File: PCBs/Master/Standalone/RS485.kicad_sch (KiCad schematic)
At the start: 16 parts, among them U4 TBU-CA065-200-WH, U5 TBU-CA065-200-WH, U6 TISP4240M3BJR-S, U7 MAX487ESA+T, U8 MAX487ESA+T, U9 TISP4240M3BJR-S

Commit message: Master WIP
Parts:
- R10: footprint Resistor_SMD:R_0805_2012Metric -> Resistor_SMD:R_0402_1005Metric; LCSC C22978 -> C25890
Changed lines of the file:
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@@
     (property "Reference" "R10" (id 0) (at 173.99 128.27 90))
     (property "Value" "3.3K" (id 1) (at 173.99 130.81 90))
-    (property "Footprint" "Resistor_SMD:R_0805_2012Metric" (id 2) (at 173.99 132.842 90)
+    (property "Footprint" "Resistor_SMD:R_0402_1005Metric" (id 2) (at 173.99 132.842 90)
       (effects (font (size 1.27 1.27)) hide)
     )
@@
       (effects (font (size 1.27 1.27)) hide)
     )
-    (property "LCSC" "C22978" (id 4) (at 173.99 134.62 0)
+    (property "LCSC" "C25890" (id 4) (at 173.99 134.62 0)
       (effects (font (size 1.27 1.27)) hide)
     )

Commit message: Master Rev. 1
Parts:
- removed U6, U9: TISP4240M3BJR-S, A10 KiCad Libraries:DO-214AA_L4.4-W3.6-LS5.3-BI, symbol A10:TISP4240M3BJR-S
- F4: footprint A10 KiCad Libraries:FUSE_BK-6013 -> A10 KiCad Libraries:FUSE-TH_XF-506P
- U4, U5: now left out of the parts list
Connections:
- net RS485+: now also D6.1 (A1), F3.1
- net RS485-: now also D6.2 (A2), F2.2
- now unconnected: U4.1 (IN/OUT), U5.3 (OUT/IN)
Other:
- moved on the sheet: U4, U5
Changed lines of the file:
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@@
   (junction (at 97.79 106.68) (diameter 0) (color 0 0 0 0)
   )
-  (no_connect (at 154.94 97.79))
-  (no_connect (at 154.94 113.03))
+  (no_connect (at 157.48 97.79))
+  (no_connect (at 157.48 113.03))
   (wire (pts (xy 143.51 96.52) (xy 154.94 95.25))
     (stroke (width 0) (type default) (color 0 0 0 0))
@@
     (stroke (width 0) (type default) (color 0 0 0 0))
   )
-  (wire (pts (xy 185.42 106.68) (xy 154.94 106.68))
-    (stroke (width 0) (type default) (color 0 0 0 0))
-  )
   (wire (pts (xy 116.84 128.27) (xy 116.84 130.81))
     (stroke (width 0) (type default) (color 0 0 0 0))
   )
-  (wire (pts (xy 154.94 106.68) (xy 154.94 110.49))
-    (stroke (width 0) (type default) (color 0 0 0 0))
-  )
   (wire (pts (xy 166.37 134.62) (xy 170.18 134.62))
     (stroke (width 0) (type default) (color 0 0 0 0))
@@
     (stroke (width 0) (type default) (color 0 0 0 0))
   )
-  (wire (pts (xy 185.42 104.14) (xy 207.01 104.14))
+  (wire (pts (xy 154.94 104.14) (xy 185.42 104.14))
     (stroke (width 0) (type default) (color 0 0 0 0))
   )
@@
     (stroke (width 0) (type default) (color 0 0 0 0))
   )
-  (wire (pts (xy 195.58 106.68) (xy 207.01 106.68))
-    (stroke (width 0) (type default) (color 0 0 0 0))
-  )
-  (wire (pts (xy 154.94 100.33) (xy 154.94 104.14))
+  (wire (pts (xy 154.94 106.68) (xy 185.42 106.68))
+    (stroke (width 0) (type default) (color 0 0 0 0))
+  )
+  (wire (pts (xy 154.94 95.25) (xy 154.94 104.14))
     (stroke (width 0) (type default) (color 0 0 0 0))
   )
@@
     (stroke (width 0) (type default) (color 0 0 0 0))
   )
+  (wire (pts (xy 154.94 106.68) (xy 154.94 115.57))
+    (stroke (width 0) (type default) (color 0 0 0 0))
+  )
   (wire (pts (xy 107.95 83.82) (xy 107.95 87.63))
     (stroke (width 0) (type default) (color 0 0 0 0))
@@
   )
   (wire (pts (xy 168.91 139.7) (xy 166.37 139.7))
-    (stroke (width 0) (type default) (color 0 0 0 0))
-  )
-  (wire (pts (xy 154.94 104.14) (xy 175.26 104.14))
     (stroke (width 0) (type default) (color 0 0 0 0))
   )
@@
     )
   )
-  (global_label "RS485+" (shape bidirectional) (at 207.01 106.68 0) (fields_autoplaced)
+  (global_label "RS485+" (shape bidirectional) (at 185.42 106.68 0) (fields_autoplaced)
     (effects (font (size 1.27 1.27)) (justify left))
-    (property "Intersheet References" "${INTERSHEET_REFS}" (id 0) (at 217.1036 106.7594 0)
+    (property "Intersheet References" "${INTERSHEET_REFS}" (id 0) (at 195.5136 106.7594 0)
       (effects (font (size 1.27 1.27)) (justify left) hide)
     )
@@
     )
   )
-  (global_label "RS485-" (shape bidirectional) (at 207.01 104.14 0) (fields_autoplaced)
+  (global_label "RS485-" (shape bidirectional) (at 185.42 104.14 0) (fields_autoplaced)
     (effects (font (size 1.27 1.27)) (justify left))
-    (property "Intersheet References" "${INTERSHEET_REFS}" (id 0) (at 217.1036 104.2194 0)
+    (property "Intersheet References" "${INTERSHEET_REFS}" (id 0) (at 195.5136 104.2194 0)
       (effects (font (size 1.27 1.27)) (justify left) hide)
     )
@@
     (effects (font (size 1.27 1.27)) (justify right))
   )
-  (hierarchical_label "RS485-" (shape output) (at 204.47 104.14 90)
+  (hierarchical_label "RS485-" (shape output) (at 182.88 104.14 90)
     (effects (font (size 1.27 1.27)) (justify left))
   )
-  (hierarchical_label "RS485+" (shape output) (at 204.47 106.68 270)
+  (hierarchical_label "RS485+" (shape output) (at 182.88 106.68 270)
     (effects (font (size 1.27 1.27)) (justify right))
   )
@@
     (pin "2")
     (pin "3")
-  )
-  (symbol (lib_id "A10:TISP4240M3BJR-S") (at 187.96 99.06 0) (unit 1)
-    (in_bom yes) (on_board yes)
-    (property "Reference" "U6" (id 0) (at 190.5 110.49 0))
-    (property "Value" "TISP4240M3BJR-S" (id 1) (at 190.5 113.03 0))
-    (property "Footprint" "A10 KiCad Libraries:DO-214AA_L4.4-W3.6-LS5.3-BI" (id 2) (at 187.96 109.22 0)
-      (effects (font (size 1.27 1.27) italic) hide)
-    )
-    (property "Datasheet" "https://atta.szlcsc.com/upload/public/pdf/source/20210316/C2760879_B8B4F1F8D05F3CAAD32384151EC07A7F.pdf" (id 3) (at 185.674 98.933 0)
-      (effects (font (size 1.27 1.27)) (justify left) hide)
-    )
-    (property "LCSC" "C840526" (id 4) (at 187.96 99.06 0)
-      (effects (font (size 1.27 1.27)) hide)
-    )
-    (pin "1")
-    (pin "2")
   )
   (symbol (lib_id "Connector_Generic:Conn_02x02_Odd_Even") (at 121.92 128.27 0) (unit 1)
@@
     (pin "4")
   )
-  (symbol (lib_name "TBU-CA065-200-WH_1") (lib_id "A10:TBU-CA065-200-WH") (at 154.94 74.93 0) (unit 1)
-    (in_bom yes) (on_board yes)
-    (property "Reference" "U4" (id 0) (at 157.48 87.63 0)
-      (effects (font (size 1.27 1.27)) (justify left))
-    )
-    (property "Value" "TBU-CA065-200-WH" (id 1) (at 157.48 90.17 0)
-      (effects (font (size 1.27 1.27)) (justify left))
-    )
-    (property "Footprint" "A10 KiCad Libraries:DIO-SMD_3P-L6.5-W4.0-BI" (id 2) (at 154.94 85.09 0)
+  (symbol (lib_name "TBU-CA065-200-WH_1") (lib_id "A10:TBU-CA065-200-WH") (at 157.48 74.93 0) (unit 1)
+    (in_bom no) (on_board no)
+    (property "Reference" "U4" (id 0) (at 160.02 87.63 0)
+      (effects (font (size 1.27 1.27)) (justify left))
+    )
+    (property "Value" "TBU-CA065-200-WH" (id 1) (at 160.02 90.17 0)
+      (effects (font (size 1.27 1.27)) (justify left))
+    )
+    (property "Footprint" "A10 KiCad Libraries:DIO-SMD_3P-L6.5-W4.0-BI" (id 2) (at 157.48 85.09 0)
       (effects (font (size 1.27 1.27) italic) hide)
     )
-    (property "Datasheet" "https://atta.szlcsc.com/upload/public/pdf/source/20200810/C720638_9C2F93931169B2F615A5326102BC91F1.pdf" (id 3) (at 152.654 74.803 0)
-      (effects (font (size 1.27 1.27)) (justify left) hide)
-    )
-    (property "LCSC" "C913221" (id 4) (at 154.94 74.93 0)
+    (property "Datasheet" "https://atta.szlcsc.com/upload/public/pdf/source/20200810/C720638_9C2F93931169B2F615A5326102BC91F1.pdf" (id 3) (at 155.194 74.803 0)
+      (effects (font (size 1.27 1.27)) (justify left) hide)
+    )
+    (property "LCSC" "C913221" (id 4) (at 157.48 74.93 0)
       (effects (font (size 1.27 1.27)) hide)
     )
@@
     (pin "8")
   )
-  (symbol (lib_id "A10:TISP4240M3BJR-S") (at 182.88 111.76 180) (unit 1)
-    (in_bom yes) (on_board yes) (fields_autoplaced)
-    (property "Reference" "U9" (id 0) (at 180.34 99.06 0))
-    (property "Value" "TISP4240M3BJR-S" (id 1) (at 180.34 101.6 0))
-    (property "Footprint" "A10 KiCad Libraries:DO-214AA_L4.4-W3.6-LS5.3-BI" (id 2) (at 182.88 101.6 0)
-      (effects (font (size 1.27 1.27) italic) hide)
-    )
-    (property "Datasheet" "https://atta.szlcsc.com/upload/public/pdf/source/20210316/C2760879_B8B4F1F8D05F3CAAD32384151EC07A7F.pdf" (id 3) (at 185.166 111.887 0)
-      (effects (font (size 1.27 1.27)) (justify left) hide)
-    )
-    (property "LCSC" "C840526" (id 4) (at 182.88 111.76 0)
-      (effects (font (size 1.27 1.27)) hide)
-    )
-    (pin "1")
-    (pin "2")
-  )
   (symbol (lib_id "power:GND") (at 124.46 87.63 90) (unit 1)
     (in_bom yes) (on_board yes) (fields_autoplaced)
@@
       (effects (font (size 1.27 1.27)) (justify left))
     )
-    (property "Footprint" "A10 KiCad Libraries:FUSE_BK-6013" (id 2) (at 140.97 136.398 90)
+    (property "Footprint" "A10 KiCad Libraries:FUSE-TH_XF-506P" (id 2) (at 140.97 136.398 90)
       (effects (font (size 1.27 1.27)) hide)
     )
@@
     (pin "8")
   )
-  (symbol (lib_name "TBU-CA065-200-WH_1") (lib_id "A10:TBU-CA065-200-WH") (at 154.94 90.17 0) (unit 1)
-    (in_bom yes) (on_board yes)
-    (property "Reference" "U5" (id 0) (at 157.48 120.65 0)
-      (effects (font (size 1.27 1.27)) (justify left))
-    )
-    (property "Value" "TBU-CA065-200-WH" (id 1) (at 157.48 123.19 0)
-      (effects (font (size 1.27 1.27)) (justify left))
-    )
-    (property "Footprint" "A10 KiCad Libraries:DIO-SMD_3P-L6.5-W4.0-BI" (id 2) (at 154.94 100.33 0)
+  (symbol (lib_name "TBU-CA065-200-WH_1") (lib_id "A10:TBU-CA065-200-WH") (at 157.48 90.17 0) (unit 1)
+    (in_bom no) (on_board no)
+    (property "Reference" "U5" (id 0) (at 160.02 120.65 0)
+      (effects (font (size 1.27 1.27)) (justify left))
+    )
+    (property "Value" "TBU-CA065-200-WH" (id 1) (at 160.02 123.19 0)
+      (effects (font (size 1.27 1.27)) (justify left))
+    )
+    (property "Footprint" "A10 KiCad Libraries:DIO-SMD_3P-L6.5-W4.0-BI" (id 2) (at 157.48 100.33 0)
       (effects (font (size 1.27 1.27) italic) hide)
     )
-    (property "Datasheet" "https://atta.szlcsc.com/upload/public/pdf/source/20200810/C720638_9C2F93931169B2F615A5326102BC91F1.pdf" (id 3) (at 152.654 90.043 0)
-      (effects (font (size 1.27 1.27)) (justify left) hide)
-    )
-    (property "LCSC" "C913221" (id 4) (at 154.94 90.17 0)
-      (effects (font (size 1.27 1.27)) hide)
-    )
+    (property "Datasheet" "https://atta.szlcsc.com/upload/public/pdf/source/20200810/C720638_9C2F93931169B2F615A5326102BC91F1.pdf" (id 3) (at 155.194 90.043 0)
+      (effects (font (size 1.27 1.27)) (justify left) hide)
+    )
+    (property "LCSC" "C913221" (id 4) (at 157.48 90.17 0)
+      (effects (font (size 1.27 1.27)) hide)
+    )

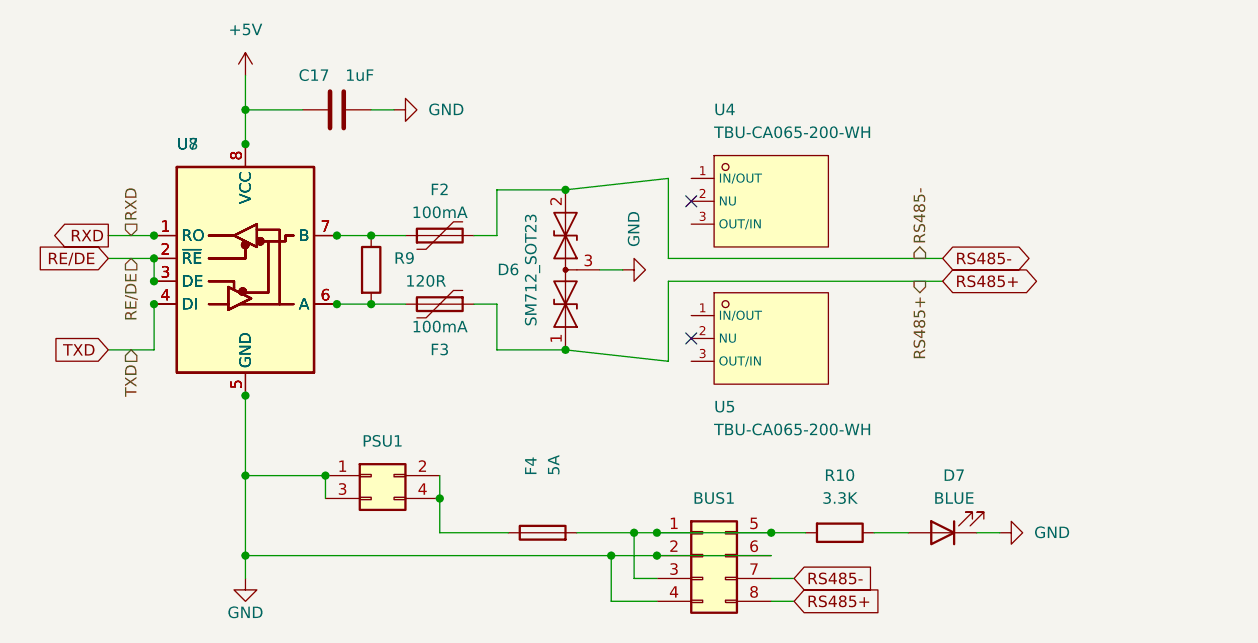
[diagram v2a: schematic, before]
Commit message: Updated Master to use PCIe Power Directly
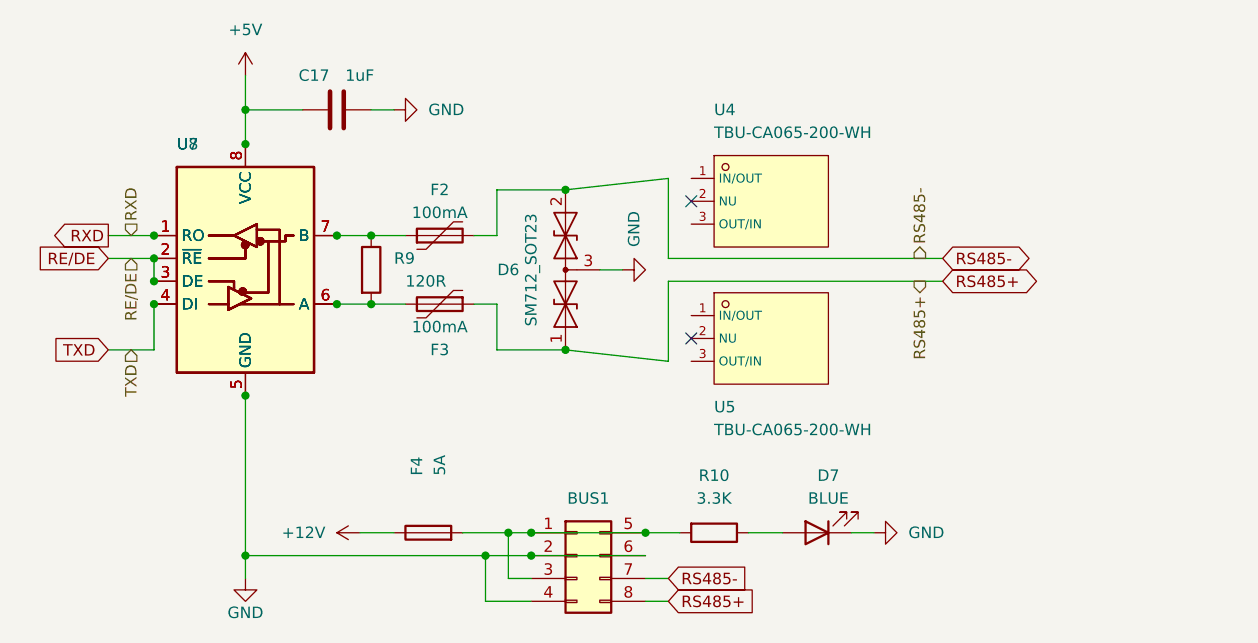
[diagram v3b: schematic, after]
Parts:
- removed PSU1: Conn_02x02_Top_Bottom, A10 KiCad Libraries:Molex Micro-Fit 3.0 43045-0400, symbol Connector_Generic:Conn_02x02_Odd_Even
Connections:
- net +12V: now reaches F4.1
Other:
- moved on the sheet: BUS1, D7, F4, R10

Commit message: Updated HUB
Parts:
- F4: now in the parts list
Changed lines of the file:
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@@
   )
   (symbol (lib_id "Device:Fuse") (at 128.27 134.62 90) (unit 1)
-    (in_bom no) (on_board yes)
+    (in_bom yes) (on_board yes)
     (property "Reference" "F4" (id 0) (at 126.9999 128.27 0)
       (effects (font (size 1.27 1.27)) (justify left))
